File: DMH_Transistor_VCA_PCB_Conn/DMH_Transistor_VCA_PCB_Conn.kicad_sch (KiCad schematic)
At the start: 0 parts

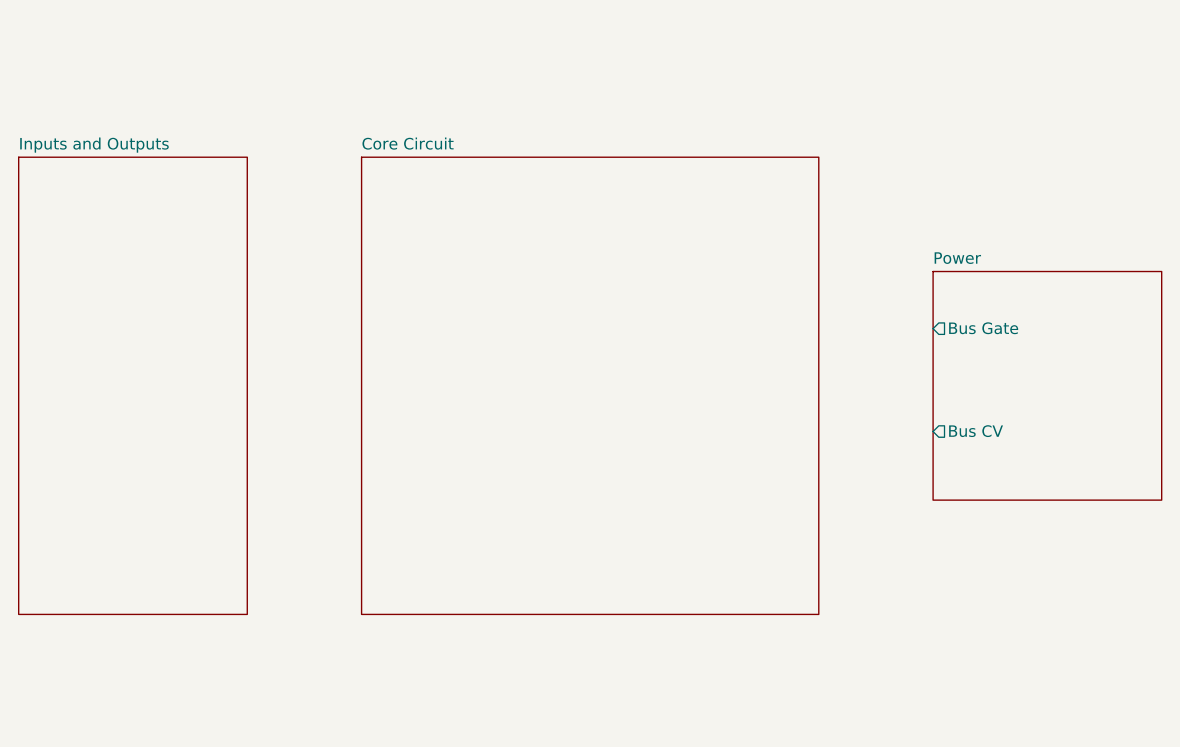
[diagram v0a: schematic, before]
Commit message: Pots PCB in progress
Need to add CV input traces to the pin headers
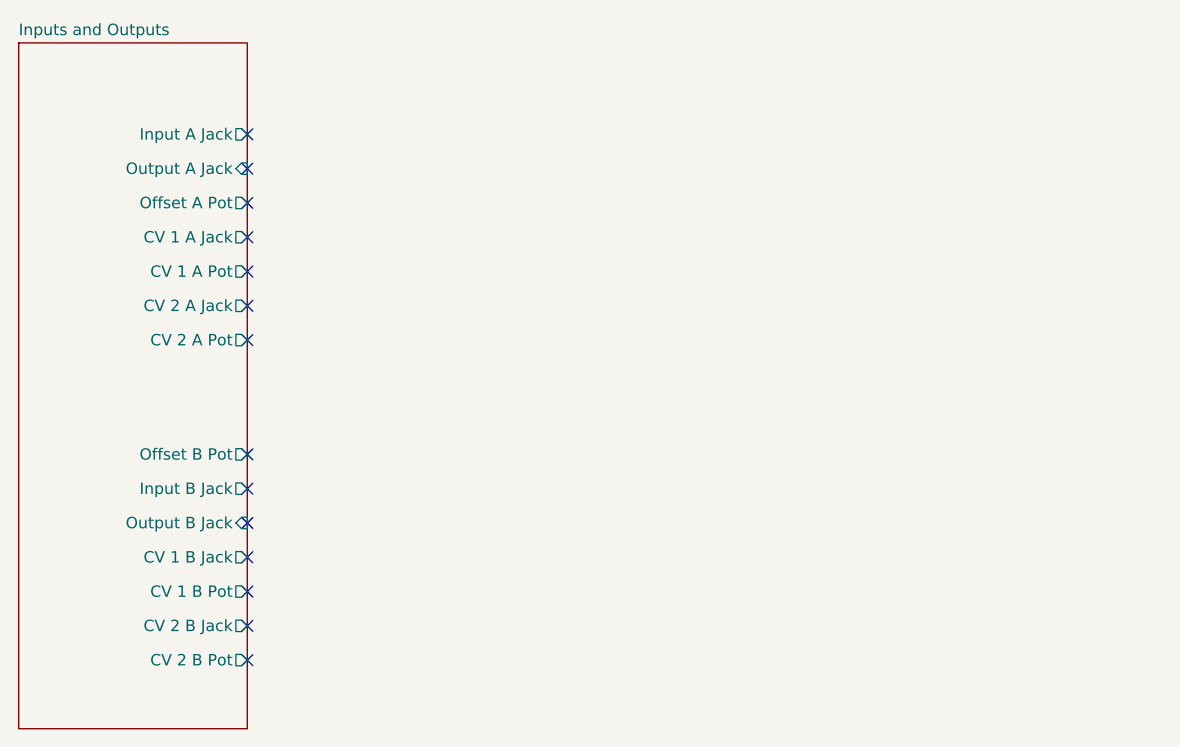
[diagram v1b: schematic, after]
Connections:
- no-connect marks 0 -> 14
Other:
- removed sheet Core Circuit
- removed sheet Power
- sheet Inputs and Outputs ports: added CV 1 A Jack, CV 1 A Pot, CV 1 B Jack, CV 1 B Pot, CV 2 A Jack, CV 2 A Pot, CV 2 B Jack, CV 2 B Pot, Input A Jack, Input B Jack, Offset A Pot, Offset B Pot, Output A Jack, Output B Jack; removed none
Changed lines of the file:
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@@
 		(comment 1 "PCB for 5 cm Kosmo format synthesizer module")
 	)
+	(no_connect
+		(at 50.8 81.28)
+	)
+	(no_connect
+		(at 50.8 124.46)
+	)
+	(no_connect
+		(at 50.8 92.71)
+	)
+	(no_connect
+		(at 50.8 88.9)
+	)
+	(no_connect
+		(at 50.8 109.22)
+	)
+	(no_connect
+		(at 50.8 116.84)
+	)
+	(no_connect
+		(at 50.8 113.03)
+	)
+	(no_connect
+		(at 50.8 73.66)
+	)
+	(no_connect
+		(at 50.8 96.52)
+	)
+	(no_connect
+		(at 50.8 132.08)
+	)
+	(no_connect
+		(at 50.8 77.47)
+	)
+	(no_connect
+		(at 50.8 85.09)
+	)
+	(no_connect
+		(at 50.8 120.65)
+	)
+	(no_connect
+		(at 50.8 128.27)
+	)
 	(sheet
-		(at 127 88.9)
-		(size 25.4 25.4)
+		(at 25.4 63.5)
+		(size 25.4 76.2)
 		(fields_autoplaced yes)
 		(stroke
@@
 			(color 0 0 0 0.0000)
 		)
-		(property "Sheetname" "Power"
-			(at 127 88.1884 0)
+		(property "Sheetname" "Inputs and Outputs"
+			(at 25.4 62.7884 0)
 			(effects
 				(font
@@
 			)
 		)
-		(property "Sheetfile" "Power.kicad_sch"
-			(at 127 114.8846 0)
+		(property "Sheetfile" "Inputs_and_Outputs.kicad_sch"
+			(at 25.4 140.2846 0)
 			(effects
 				(font
@@
 			)
 		)
-		(pin "Bus Gate" output
-			(at 127 95.25 180)
-			(effects
-				(font
-					(size 1.27 1.27)
-				)
-				(justify left)
-			)
-		)
-		(pin "Bus CV" output
-			(at 127 106.68 180)
-			(effects
-				(font
-					(size 1.27 1.27)
-				)
-				(justify left)
+		(pin "Output A Jack" input
+			(at 50.8 77.47 0)
+			(effects
+				(font
+					(size 1.27 1.27)
+				)
+				(justify right)
+			)
+		)
+		(pin "Input A Jack" output
+			(at 50.8 73.66 0)
+			(effects
+				(font
+					(size 1.27 1.27)
+				)
+				(justify right)
+			)
+		)
+		(pin "CV 1 A Jack" output
+			(at 50.8 85.09 0)
+			(effects
+				(font
+					(size 1.27 1.27)
+				)
+				(justify right)
+			)
+		)
+		(pin "CV 2 A Pot" output
+			(at 50.8 96.52 0)
+			(effects
+				(font
+					(size 1.27 1.27)
+				)
+				(justify right)
+			)
+		)
+		(pin "Offset A Pot" output
+			(at 50.8 81.28 0)
+			(effects
+				(font
+					(size 1.27 1.27)
+				)
+				(justify right)
+			)
+		)
+		(pin "CV 1 A Pot" output
+			(at 50.8 88.9 0)
+			(effects
+				(font
+					(size 1.27 1.27)
+				)
+				(justify right)
+			)
+		)
+		(pin "CV 2 A Jack" output
+			(at 50.8 92.71 0)
+			(effects
+				(font
+					(size 1.27 1.27)
+				)
+				(justify right)
+			)
+		)
+		(pin "CV 1 B Jack" output
+			(at 50.8 120.65 0)
+			(effects
+				(font
+					(size 1.27 1.27)
+				)
+				(justify right)
+			)
+		)
+		(pin "CV 1 B Pot" output
+			(at 50.8 124.46 0)
+			(effects
+				(font
+					(size 1.27 1.27)
+				)
+				(justify right)
+			)
+		)
+		(pin "CV 2 B Pot" output
+			(at 50.8 132.08 0)
+			(effects
+				(font
+					(size 1.27 1.27)
+				)
+				(justify right)
+			)
+		)
+		(pin "Offset B Pot" output
+			(at 50.8 109.22 0)
+			(effects
+				(font
+					(size 1.27 1.27)
+				)
+				(justify right)
+			)
+		)
+		(pin "Input B Jack" output
+			(at 50.8 113.03 0)
+			(effects
+				(font
+					(size 1.27 1.27)
+				)
+				(justify right)
+			)
+		)
+		(pin "CV 2 B Jack" output
+			(at 50.8 128.27 0)
+			(effects
+				(font
+					(size 1.27 1.27)
+				)
+				(justify right)
+			)
+		)
+		(pin "Output B Jack" input
+			(at 50.8 116.84 0)
+			(effects
+				(font
+					(size 1.27 1.27)
+				)
+				(justify right)
 			)
 		)
 		(instances
-			(project "DMH-Kosmo-5cm-PCB"
-				(path "/58f4306d-5387-4983-bb08-41a2313fd315"
-					(page "4")
-				)
-			)
-		)
-	)
-	(sheet
-		(at 63.5 76.2)
-		(size 50.8 50.8)
-		(fields_autoplaced yes)
-		(stroke
-			(width 0.1524)
-			(type solid)
-		)
-		(fill
-			(color 0 0 0 0.0000)
-		)
-		(property "Sheetname" "Core Circuit"
-			(at 63.5 75.4884 0)
-			(effects
-				(font
-					(size 1.27 1.27)
-				)
-				(justify left bottom)
-			)
-		)
-		(property "Sheetfile" "Core_Circuit.kicad_sch"
-			(at 63.5 127.5846 0)
-			(effects
-				(font
-					(size 1.27 1.27)
-				)
-				(justify left top)
-				(hide yes)
-			)
-		)
-		(instances
-			(project "DMH-Kosmo-5cm-PCB"
-				(path "/58f4306d-5387-4983-bb08-41a2313fd315"
-					(page "3")
-				)
-			)
-		)
-	)
-	(sheet
-		(at 25.4 76.2)
-		(size 25.4 50.8)
-		(fields_autoplaced yes)
-		(stroke
-			(width 0.1524)
-			(type solid)
-		)
-		(fill
-			(color 0 0 0 0.0000)
-		)
-		(property "Sheetname" "Inputs and Outputs"
-			(at 25.4 75.4884 0)
-			(effects
-				(font
-					(size 1.27 1.27)
-				)
-				(justify left bottom)
-			)
-		)
-		(property "Sheetfile" "Inputs_and_Outputs.kicad_sch"
-			(at 25.4 127.5846 0)
-			(effects
-				(font
-					(size 1.27 1.27)
-				)
-				(justify left top)
-				(hide yes)
-			)
-		)
-		(instances
-			(project "DMH-Kosmo-5cm-PCB"
+			(project "DMH_Transistor_VCA_PCB_Conn"
 				(path "/58f4306d-5387-4983-bb08-41a2313fd315"
 					(page "2")
